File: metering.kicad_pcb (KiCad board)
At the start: 2 copper layers, 75 x 86 mm, 61 parts, among them J1 Conn_01x08, J2 USB_C_Receptacle_USB2.0_16P, J3 Prog, P1 Conn_01x08, SW1 Reset, SW2 Boot, U1 USBLC6-2SC6, U2 AMS1117-3.3, U3 ESP32-C3-WROOM-02U, U4 74HC14, X1 Screw_Terminal_01x06, X2 Screw_Terminal_01x06, Y1 32.768kHz

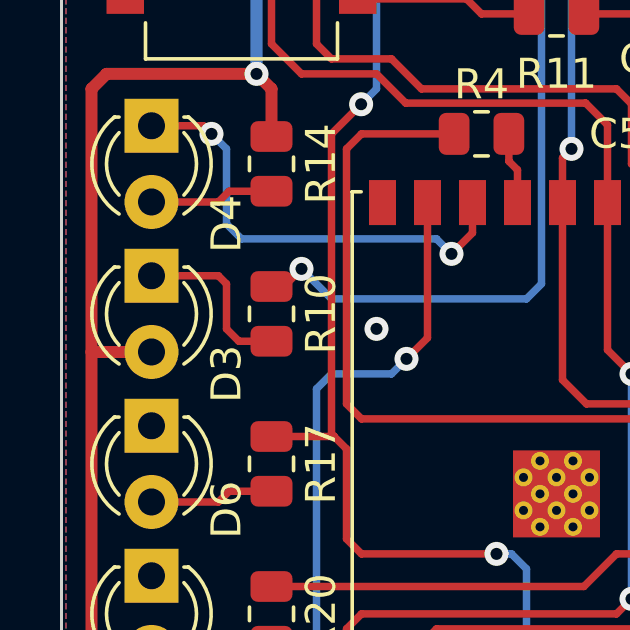
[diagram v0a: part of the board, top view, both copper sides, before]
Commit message: Fix UART LED polarity to not light up during idle Rx (high level)
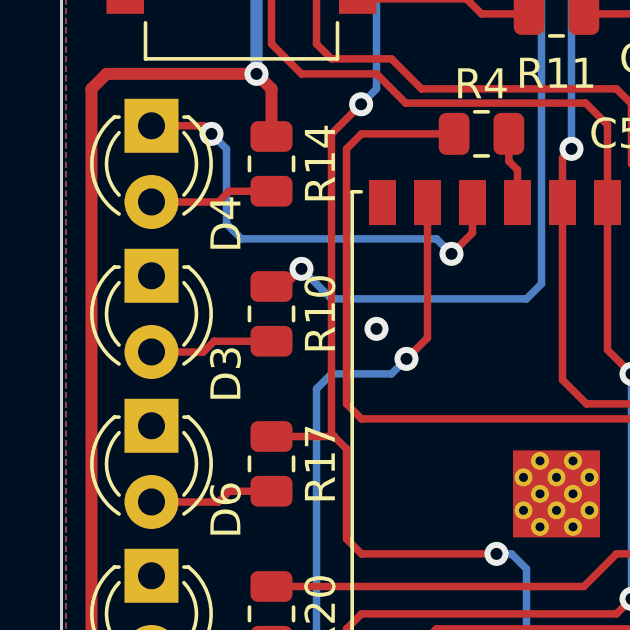
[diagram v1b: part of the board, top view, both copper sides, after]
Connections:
- D3 pad 1: Net-(D3-K) -> GND
- D3 pad 2: +3.3V -> Net-(D3-A)
- R10 pad 2: Net-(D3-K) -> Net-(D3-A)
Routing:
- net Net-(D3-K): track 5.78 -> 0.00 mm
- net Net-(D3-A): track 0.00 -> 4.15 mm
- net +3.3V: track 190.4 -> 188.4 mm
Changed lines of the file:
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@@
 	(title_block
 		(title "Smart Home Energy Metering")
-		(date "2025-07-10")
+		(date "2025-07-15")
 		(rev "1.2-dev")
 		(comment 1 "https://github.com/zargony/smarthome-metering")
@@
 	(net 14 "Net-(D7-K)")
 	(net 15 "Net-(D9-K)")
-	(net 16 "Net-(D3-K)")
+	(net 16 "Net-(D3-A)")
 	(net 17 "Net-(D4-A)")
 	(net 18 "/IO8")
@@
 			)
 		)
-		(property "Datasheet" ""
+		(property "Datasheet" "~"
 			(at 0 0 0)
 			(layer "F.Fab")
@@
 			)
 		)
-		(property "Datasheet" ""
+		(property "Datasheet" "~"
 			(at 0 0 0)
 			(layer "F.Fab")
@@
 			)
 		)
-		(property "Datasheet" ""
+		(property "Datasheet" "~"
 			(at 0 0 90)
 			(layer "F.Fab")
@@
 			)
 		)
-		(property "Datasheet" ""
+		(property "Datasheet" "~"
 			(at 0 0 0)
 			(layer "F.Fab")
@@
 			)
 		)
-		(property "Datasheet" ""
+		(property "Datasheet" "~"
 			(at 0 0 0)
 			(unlocked yes)
@@
 			)
 		)
-		(property "Datasheet" ""
+		(property "Datasheet" "~"
 			(at 0 0 90)
 			(layer "F.Fab")
@@
 			)
 		)
-		(property "Datasheet" ""
+		(property "Datasheet" "~"
 			(at 0 0 90)
 			(layer "F.Fab")
@@
 			)
 		)
-		(property "Datasheet" ""
+		(property "Datasheet" "~"
 			(at 0 0 180)
 			(unlocked yes)
@@
 			)
 		)
-		(property "Datasheet" ""
+		(property "Datasheet" "~"
 			(at 0 0 0)
 			(layer "F.Fab")
@@
 			)
 		)
-		(property "Datasheet" ""
+		(property "Datasheet" "~"
 			(at 0 0 0)
 			(layer "F.Fab")
@@
 			)
 		)
-		(property "Datasheet" ""
+		(property "Datasheet" "~"
 			(at 0 0 90)
 			(layer "F.Fab")
@@
 			)
 		)
-		(property "Datasheet" ""
+		(property "Datasheet" "~"
 			(at 0 0 0)
 			(layer "F.Fab")
@@
 			)
 		)
-		(property "Datasheet" ""
+		(property "Datasheet" "~"
 			(at 0 0 90)
 			(layer "F.Fab")
@@
 			)
 		)
-		(property "Datasheet" ""
+		(property "Datasheet" "~"
 			(at 0 0 0)
 			(layer "F.Fab")
@@
 			)
 		)
-		(property "Datasheet" ""
+		(property "Datasheet" "~"
 			(at 0 0 0)
 			(layer "F.Fab")
@@
 			)
 		)
-		(property "Datasheet" ""
+		(property "Datasheet" "~"
 			(at 0 0 90)
 			(layer "F.Fab")
@@
 			)
 		)
-		(property "Datasheet" ""
+		(property "Datasheet" "~"
 			(at 0 0 0)
 			(layer "F.Fab")
@@
 			)
 		)
-		(property "Datasheet" ""
+		(property "Datasheet" "~"
 			(at 0 0 0)
 			(layer "F.Fab")
@@
 			)
 		)
-		(property "Datasheet" ""
+		(property "Datasheet" "~"
 			(at 0 0 0)
 			(layer "F.Fab")
@@
 			)
 		)
-		(property "Datasheet" ""
+		(property "Datasheet" "~"
 			(at 0 0 0)
 			(layer "F.Fab")
@@
 			)
 		)
-		(property "Datasheet" ""
+		(property "Datasheet" "~"
 			(at 0 0 90)
 			(layer "F.Fab")
@@
 			(layers "*.Cu" "*.Mask")
 			(remove_unused_layers no)
-			(net 16 "Net-(D3-K)")
+			(net 1 "GND")
 			(pinfunction "K")
 			(pintype "passive")
@@
 			(layers "*.Cu" "*.Mask")
 			(remove_unused_layers no)
-			(net 2 "+3.3V")
+			(net 16 "Net-(D3-A)")
 			(pinfunction "A")
 			(pintype "passive")
@@
 			)
 		)
-		(property "Datasheet" ""
+		(property "Datasheet" "~"
 			(at 0 0 90)
 			(layer "F.Fab")
@@
 			)
 		)
-		(property "Datasheet" ""
+		(property "Datasheet" "~"
 			(at 0 0 90)
 			(layer "F.Fab")
@@
 			)
 		)
-		(property "Datasheet" ""
+		(property "Datasheet" "~"
 			(at 0 0 90)
 			(layer "F.Fab")
@@
 			)
 		)
-		(property "Datasheet" ""
+		(property "Datasheet" "~"
 			(at 0 0 0)
 			(layer "F.Fab")
@@
 			)
 		)
-		(property "Datasheet" ""
+		(property "Datasheet" "~"
 			(at 0 0 90)
 			(layer "F.Fab")
@@
 			(layers "F.Cu" "F.Mask" "F.Paste")
 			(roundrect_rratio 0.243902)
-			(net 16 "Net-(D3-K)")
+			(net 16 "Net-(D3-A)")
 			(pintype "passive")
 		)
@@
 			)
 		)
-		(property "Datasheet" ""
+		(property "Datasheet" "~"
 			(at 0 0 90)
 			(layer "F.Fab")
@@
 			)
 		)
-		(property "Datasheet" ""
+		(property "Datasheet" "~"
 			(at 0 0 0)
 			(layer "F.Fab")
@@
 			)
 		)
-		(property "Datasheet" ""
+		(property "Datasheet" "~"
 			(at 0 0 90)
 			(layer "F.Fab")
@@
 			)
 		)
-		(property "Datasheet" ""
+		(property "Datasheet" "~"
 			(at 0 0 0)
 			(layer "F.Fab")
@@
 			)
 		)
-		(property "Datasheet" ""
+		(property "Datasheet" "~"
 			(at 0 0 90)
 			(layer "F.Fab")
@@
 			)
 		)
-		(property "Datasheet" ""
+		(property "Datasheet" "~"
 			(at 0 0 0)
 			(layer "F.Fab")
@@
 			)
 		)
-		(property "Datasheet" ""
+		(property "Datasheet" "~"
 			(at 0 0 90)
 			(layer "F.Fab")
@@
 			)
 		)
-		(property "Datasheet" ""
+		(property "Datasheet" "~"
 			(at 0 0 0)
 			(layer "F.Fab")
@@
 			)
 		)
-		(property "Datasheet" ""
+		(property "Datasheet" "~"
 			(at 0 0 90)
 			(layer "F.Fab")
@@
 			)
 		)
-		(property "Datasheet" ""
+		(property "Datasheet" "~"
 			(at 0 0 90)
 			(layer "F.Fab")
@@
 			)
 		)
-		(property "Datasheet" ""
+		(property "Datasheet" "~"
 			(at 0 0 90)
 			(layer "F.Fab")
@@
 			)
 		)
-		(property "Datasheet" ""
+		(property "Datasheet" "~"
 			(at 0 0 0)
 			(layer "F.Fab")
@@
 			)
 		)
-		(property "Datasheet" ""
+		(property "Datasheet" "~"
 			(at 0 0 0)
 			(layer "F.Fab")
@@
 			)
 		)
-		(property "Datasheet" ""
+		(property "Datasheet" "~"
 			(at 0 0 90)
 			(layer "F.Fab")
@@
 			)
 		)
-		(property "Datasheet" ""
+		(property "Datasheet" "~"
 			(at 0 0 90)
 			(layer "F.Fab")
@@
 			)
 		)
-		(property "Datasheet" ""
+		(property "Datasheet" "~"
 			(at 0 0 270)
 			(unlocked yes)
@@
 			)
 		)
-		(property "Datasheet" ""
+		(property "Datasheet" "~"
 			(at 0 0 0)
 			(layer "F.Fab")
@@
 			)
 		)
-		(property "Datasheet" ""
+		(property "Datasheet" "~"
 			(at 0 0 90)
 			(layer "F.Fab")
@@
 			)
 		)
-		(property "Datasheet" ""
+		(property "Datasheet" "~"
 			(at 0 0 0)
 			(layer "F.Fab")
@@
 			)
 		)
-		(property "Datasheet" ""
+		(property "Datasheet" "~"
 			(at 0 0 0)
 			(layer "F.Fab")
@@
 			)
 		)
-		(property "Datasheet" ""
+		(property "Datasheet" "~"
 			(at 0 0 90)
 			(layer "F.Fab")
@@
 			)
 		)
-		(property "Datasheet" ""
+		(property "Datasheet" "~"
 			(at 0 0 90)
 			(layer "F.Fab")
@@
 			)
 		)
-		(property "Datasheet" ""
+		(property "Datasheet" "~"
 			(at 0 0 90)
 			(layer "F.Fab")
@@
 			)
 		)
-		(property "Datasheet" ""
+		(property "Datasheet" "~"
 			(at 0 0 90)
 			(layer "F.Fab")
@@
 			)
 		)
-		(property "Datasheet" ""
+		(property "Datasheet" "~"
 			(at 0 0 0)
 			(layer "F.Fab")
@@
 	)
 	(segment
-		(start 44.5 96.27)
-		(end 42.5 96.27)
-		(width 0.4)
-		(layer "F.Cu")
-		(net 2)
-	)
-	(segment
 		(start 70 74.5)
 		(end 70 75.5)
@@
 	)
 	(segment
-		(start 44.5 93.73)
-		(end 46.73 93.73)
-		(width 0.25)
-		(layer "F.Cu")
-		(net 16)
-	)
-	(segment
-		(start 48.5 95.9125)
-		(end 47.4125 95.9125)
-		(width 0.25)
-		(layer "F.Cu")
-		(net 16)
-	)
-	(segment
-		(start 47.4125 95.9125)
-		(end 47 95.5)
+		(start 44.5 96.27)
+		(end 46.23 96.27)
 		(width 0.25)
 		(layer "F.Cu")
@@
 	)
 	(segment
-		(start 47 94)
-		(end 47 95.5)
+		(start 46.23 96.27)
+		(end 46.5875 95.9125)
 		(width 0.25)
 		(layer "F.Cu")
@@
 	)
 	(segment
-		(start 46.73 93.73)
-		(end 47 94)
+		(start 46.5875 95.9125)
+		(end 48.5 95.9125)
 		(width 0.25)
 		(layer "F.Cu")

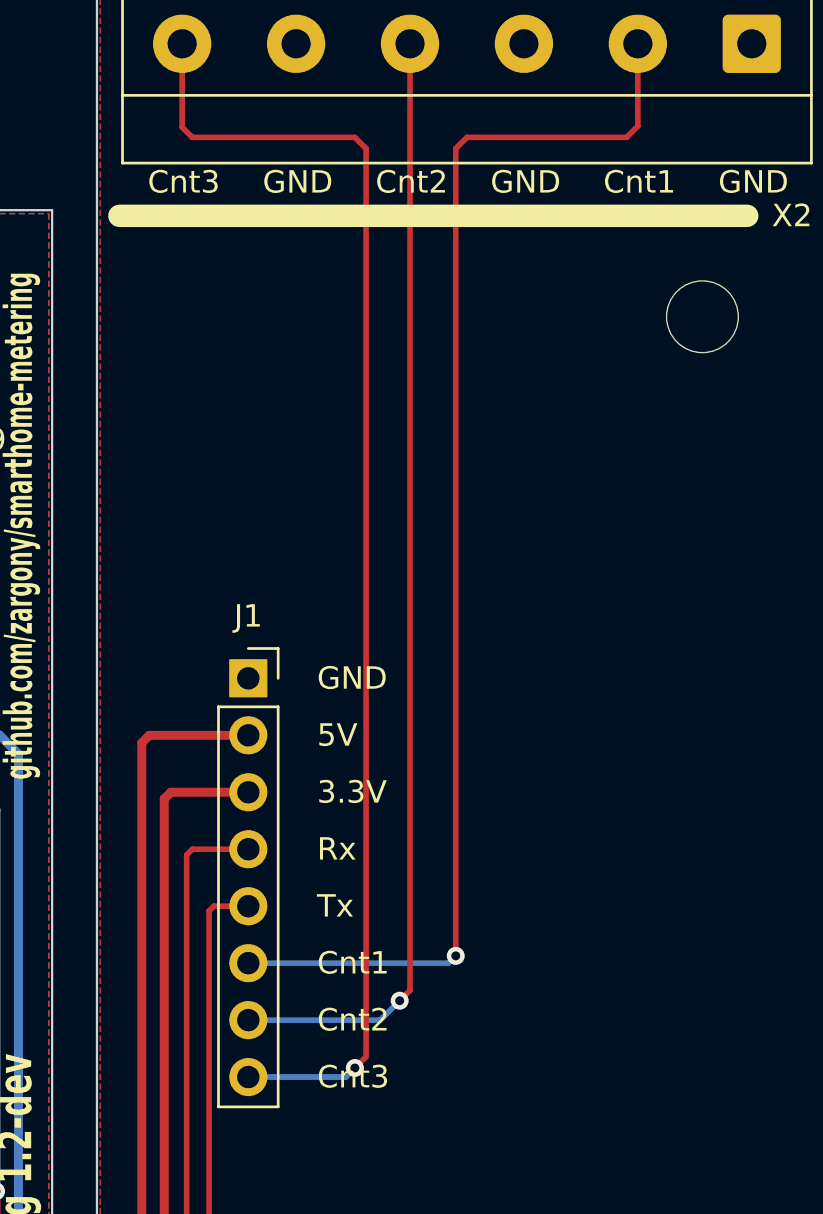
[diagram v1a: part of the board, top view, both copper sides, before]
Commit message: Re-route contacts to fix order on terminal header
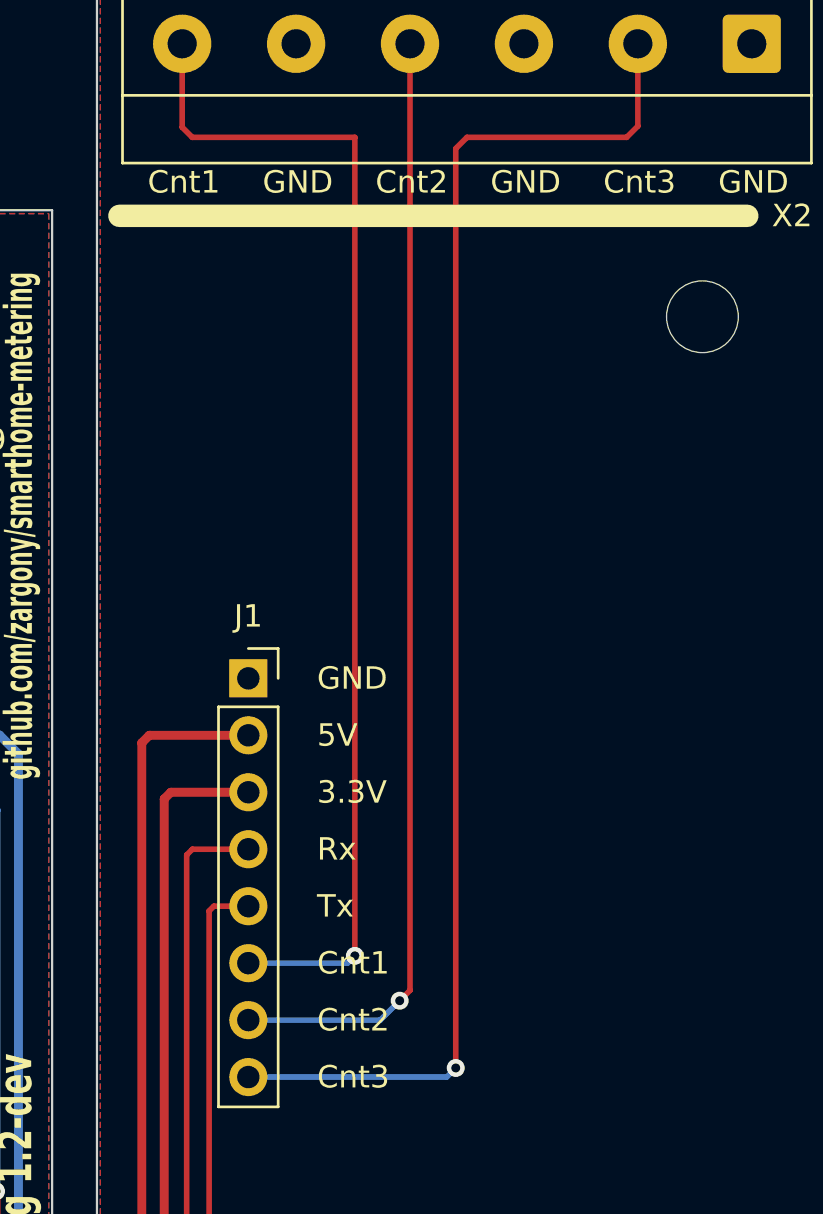
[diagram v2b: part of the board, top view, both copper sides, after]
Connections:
- X2 pad 2: Net-(J1-Pin_6) -> Net-(J1-Pin_8)
- X2 pad 6: Net-(J1-Pin_8) -> Net-(J1-Pin_6)
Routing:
- net Net-(J1-Pin_6): track 57.6 -> 53.0 mm
- net Net-(J1-Pin_8): track 58.4 -> 62.6 mm
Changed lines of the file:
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@@
 	(title_block
 		(title "Smart Home Energy Metering")
-		(date "2025-07-15")
+		(date "2025-08-01")
 		(rev "1.2-dev")
 		(comment 1 "https://github.com/zargony/smarthome-metering")
@@
 			(layers "*.Cu" "*.Mask")
 			(remove_unused_layers no)
-			(net 47 "Net-(J1-Pin_6)")
+			(net 48 "Net-(J1-Pin_8)")
 			(pinfunction "Pin_2")
 			(pintype "passive")
@@
 			(layers "*.Cu" "*.Mask")
 			(remove_unused_layers no)
-			(net 48 "Net-(J1-Pin_8)")
+			(net 47 "Net-(J1-Pin_6)")
 			(pinfunction "Pin_6")
 			(pintype "passive")
@@
 		)
 	)
-	(gr_text "Cnt1"
+	(gr_text "Cnt3"
 		(at 107.696 69 0)
 		(layer "F.SilkS")
@@
 		)
 	)
-	(gr_text "Cnt3"
+	(gr_text "Cnt1"
 		(at 87.376 69 0)
 		(layer "F.SilkS")
@@
 	)
 	(segment
-		(start 107.62 66.5)
-		(end 107.62 62.8275)
-		(width 0.25)
-		(layer "F.Cu")
-		(net 47)
-	)
-	(segment
-		(start 100 67)
-		(end 107.12 67)
+		(start 87.75 67)
+		(end 95 67)
 		(width 0.25)
 		(layer "F.Cu")
@@
 	)
 	(segment
-		(start 99.5 103.5)
-		(end 99.5 67.5)
+		(start 95 67)
+		(end 95 103.5)
 		(width 0.25)
 		(layer "F.Cu")
@@
 	)
 	(segment
-		(start 99.5 67.5)
-		(end 100 67)
+		(start 87.3 62.8275)
+		(end 87.3 66.55)
 		(width 0.25)
 		(layer "F.Cu")
@@
 	)
 	(segment
-		(start 107.12 67)
-		(end 107.62 66.5)
+		(start 87.3 66.55)
+		(end 87.75 67)
 		(width 0.25)
 		(layer "F.Cu")
@@
 	)
 	(via
-		(at 99.5 103.5)
+		(at 95 103.5)
 		(size 0.8)
 		(drill 0.4)
@@
 	)
 	(segment
-		(start 99.175 103.825)
-		(end 90.25 103.825)
+		(start 90.25 103.825)
+		(end 94.675 103.825)
 		(width 0.25)
 		(layer "B.Cu")
@@
 	)
 	(segment
-		(start 99.5 103.5)
-		(end 99.175 103.825)
+		(start 94.675 103.825)
+		(end 95 103.5)
 		(width 0.25)
 		(layer "B.Cu")
@@
 	)
 	(segment
-		(start 95 67)
-		(end 95.5 67.5)
-		(width 0.25)
-		(layer "F.Cu")
-		(net 48)
-	)
-	(segment
-		(start 87.75 67)
-		(end 95 67)
+		(start 107.12 67)
+		(end 107.62 66.5)
 		(width 0.25)
 		(layer "F.Cu")
@@
 	)
 	(segment
-		(start 95.5 67.5)
-		(end 95.5 108)
+		(start 107.62 66.5)
+		(end 107.62 62.8275)
 		(width 0.25)
 		(layer "F.Cu")
@@
 	)
 	(segment
-		(start 87.3 66.55)
-		(end 87.75 67)
+		(start 99.5 108.5)
+		(end 99.5 67.5)
 		(width 0.25)
 		(layer "F.Cu")
@@
 	)
 	(segment
-		(start 87.3 62.8275)
-		(end 87.3 66.55)
+		(start 100 67)
+		(end 107.12 67)
 		(width 0.25)
 		(layer "F.Cu")
@@
 	)
 	(segment
-		(start 95.5 108)
-		(end 95 108.5)
+		(start 99.5 67.5)
+		(end 100 67)
 		(width 0.25)
 		(layer "F.Cu")
@@
 	)
 	(via
-		(at 95 108.5)
+		(at 99.5 108.5)
 		(size 0.8)
 		(drill 0.4)
@@
 	(segment
 		(start 90.25 108.905)
-		(end 94.595 108.905)
+		(end 99.095 108.905)
 		(width 0.25)
 		(layer "B.Cu")
@@
 	)
 	(segment
-		(start 94.595 108.905)
-		(end 95 108.5)
+		(start 99.095 108.905)
+		(end 99.5 108.5)
 		(width 0.25)
 		(layer "B.Cu")
